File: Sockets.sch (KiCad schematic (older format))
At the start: 53 parts

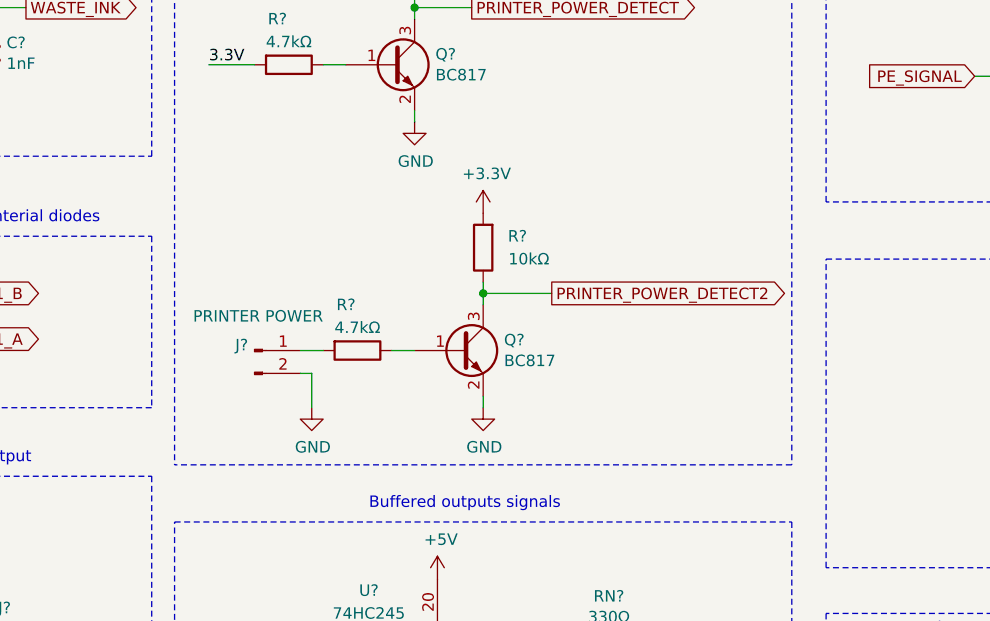
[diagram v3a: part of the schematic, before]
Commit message: Added USB B socket with ESD filter
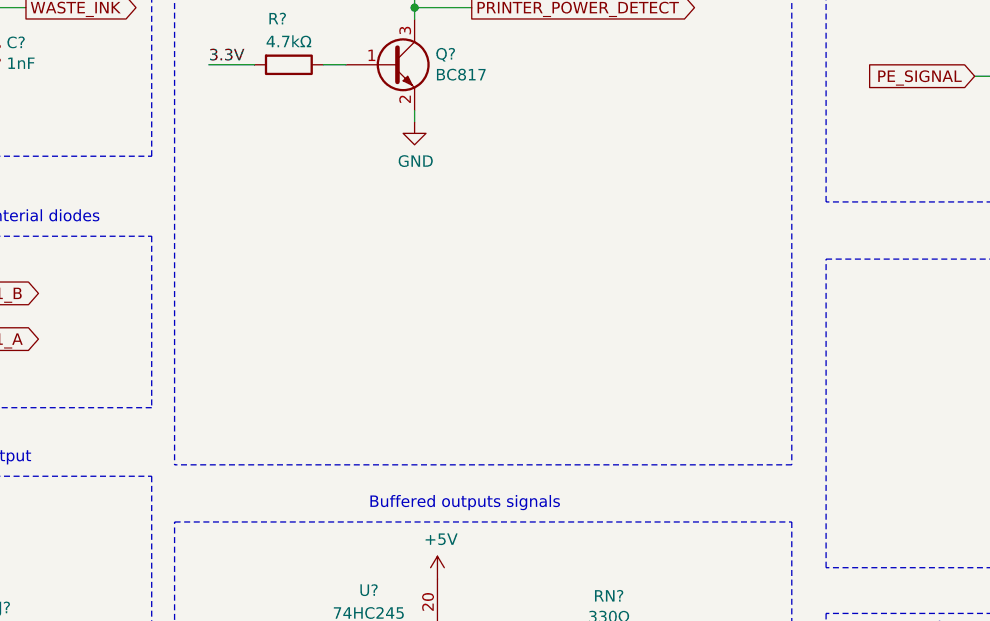
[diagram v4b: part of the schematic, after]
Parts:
- removed J?: PRINTER POWER, Connector_JST:JST_PH_B2B-PH-K_1x02_P2.00mm_Vertical, symbol Connector:Conn_01x02_Male
- removed Q?: BC817, Package_TO_SOT_SMD:SOT-23, symbol Transistor_BJT:BC817
- removed R?: 10kΩ, symbol Device:R
- removed R?: 4.7kΩ, symbol Device:R
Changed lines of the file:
@@
 	-1   0    0    -1
 $EndComp
-Text GLabel 2550 2650 2    50   Output ~ 0
-LIMIT_Y_FRONT
-Text GLabel 2500 3900 2    50   Output ~ 0
-LIMIT_Z_UP
-Text GLabel 2500 5150 2    50   Output ~ 0
-LIMIT_Z_DOWN
 Wire Wire Line
 	4500 3850 4550 3850
@@
 Text Label 2600 7000 0    50   ~ 0
 PE
-Wire Wire Line
-	6250 3000 6250 3150
-Wire Wire Line
-	6200 3000 6250 3000
-$Comp
-L power:GND #PWR?
-U 1 1 5E178011
-P 6250 3150
-AR Path="/5E07245F/5E178011" Ref="#PWR?"  Part="1"
-AR Path="/5E858220/5E178011" Ref="#PWR?"  Part="1"
-F 0 "#PWR?" H 6250 2900 50  0001 C CNN
-F 1 "GND" H 6255 2977 50  0000 C CNN
-F 2 "" H 6250 3150 50  0001 C CNN
-F 3 "" H 6250 3150 50  0001 C CNN
-	1    6250 3150
-	1    0    0    -1
-$EndComp
-Wire Wire Line
-	6200 2900 6300 2900
-Text GLabel 7300 2650 2    50   Output ~ 0
-PRINTER_POWER_DETECT2
-$Comp
-L power:+3.3V #PWR?
-U 1 1 5E168635
-P 7000 2300
-AR Path="/5E07245F/5E168635" Ref="#PWR?"  Part="1"
-AR Path="/5E858220/5E168635" Ref="#PWR?"  Part="1"
-F 0 "#PWR?" H 7000 2150 50  0001 C CNN
-F 1 "+3.3V" H 7015 2473 50  0000 C CNN
-F 2 "" H 7000 2300 50  0001 C CNN
-F 3 "" H 7000 2300 50  0001 C CNN
-	1    7000 2300
-	1    0    0    -1
-$EndComp
-$Comp
-L Device:R R?
-U 1 1 5E168627
-P 6450 2900
-AR Path="/5E07245F/5E168627" Ref="R?"  Part="1"
-AR Path="/5E858220/5E168627" Ref="R?"  Part="1"
-F 0 "R?" V 6250 2850 50  0000 C CNN
-F 1 "4.7kΩ" V 6350 2900 50  0000 C CNN
-F 2 "" V 6380 2900 50  0001 C CNN
-F 3 "~" H 6450 2900 50  0001 C CNN
-	1    6450 2900
-	0    1    1    0
-$EndComp
-Wire Wire Line
-	7000 2650 7000 2700
-Connection ~ 7000 2650
-Wire Wire Line
-	7000 2650 7300 2650
-$Comp
-L power:GND #PWR?
-U 1 1 5E16860A
-P 7000 3150
-AR Path="/5E07245F/5E16860A" Ref="#PWR?"  Part="1"
-AR Path="/5E858220/5E16860A" Ref="#PWR?"  Part="1"
-F 0 "#PWR?" H 7000 2900 50  0001 C CNN
-F 1 "GND" H 7005 2977 50  0000 C CNN
-F 2 "" H 7000 3150 50  0001 C CNN
-F 3 "" H 7000 3150 50  0001 C CNN
-	1    7000 3150
-	1    0    0    -1
-$EndComp
-Wire Wire Line
-	7000 2600 7000 2650
-$Comp
-L Device:R R?
-U 1 1 5E1685FF
-P 7000 2450
-AR Path="/5E07245F/5E1685FF" Ref="R?"  Part="1"
-AR Path="/5E858220/5E1685FF" Ref="R?"  Part="1"
-F 0 "R?" H 6850 2400 50  0000 C CNN
-F 1 "10kΩ" H 6800 2500 50  0000 C CNN
-F 2 "" V 6930 2450 50  0001 C CNN
-F 3 "~" H 7000 2450 50  0001 C CNN
-	1    7000 2450
-	-1   0    0    1
-$EndComp
-$Comp
-L Connector:Conn_01x02_Male J?
-U 1 1 5E10548D
-P 6000 2900
-AR Path="/5E07245F/5E10548D" Ref="J?"  Part="1"
-AR Path="/5E858220/5E10548D" Ref="J?"  Part="1"
-F 0 "J?" H 5972 2924 50  0000 R CNN
-F 1 "PRINTER POWER" H 6300 3050 50  0000 R CNN
-F 2 "Connector_JST:JST_PH_B2B-PH-K_1x02_P2.00mm_Vertical" H 6000 2900 50  0001 C CNN
-F 3 "~" H 6000 2900 50  0001 C CNN
-	1    6000 2900
-	1    0    0    -1
-$EndComp
-Text GLabel 6950 1400 2    50   Output ~ 0
-PRINTER_POWER_DETECT
 $Comp
 L power:+3.3V #PWR?
@@
 	1    0    0    -1
 $EndComp
-Text GLabel 2550 1400 2    50   Output ~ 0
-LIMIT_Y_BACK
 $Comp
 L Connector:Conn_01x02_Male J?
@@
 Wire Wire Line
 	9550 1700 9650 1700
-$Comp
-L Transistor_BJT:BC817 Q?
-U 1 1 5E1685F5
-P 6900 2900
-AR Path="/5E07245F/5E1685F5" Ref="Q?"  Part="1"
-AR Path="/5E858220/5E1685F5" Ref="Q?"  Part="1"
-F 0 "Q?" H 7091 2946 50  0000 L CNN
-F 1 "BC817" H 7091 2855 50  0000 L CNN
-F 2 "Package_TO_SOT_SMD:SOT-23" H 7100 2825 50  0001 L CIN
-F 3 "http://www.fairchildsemi.com/ds/BC/BC817.pdf" H 6900 2900 50  0001 L CNN
-	1    6900 2900
-	1    0    0    -1
-$EndComp
-Wire Wire Line
-	6600 2900 6700 2900
-Wire Wire Line
-	7000 3100 7000 3150
 Wire Wire Line
 	6300 1650 6400 1650
@@
 	0    -1   -1   0
 $EndComp
+Text GLabel 2550 1400 2    50   Output ~ 0
+LIMIT_Y_BACK
+Text GLabel 2500 5150 2    50   Output ~ 0
+LIMIT_Z_DOWN
+Text GLabel 2500 3900 2    50   Output ~ 0
+LIMIT_Z_UP
+Text GLabel 2550 2650 2    50   Output ~ 0
+LIMIT_Y_FRONT
+Text GLabel 6950 1400 2    50   Output ~ 0
+PRINTER_POWER_DETECT
 $EndSCHEMATC

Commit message: Improve schematics add new elements
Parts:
- removed D?: BZT52C3V3-7-F, Diode_SMD:D_SOD-123, symbol Device:D_Zener_ALT
- removed F?: SN010-60, Fuse:Fuse_1206_3216Metric, symbol Device:Polyfuse
- removed J?: PHOTO SENSOR EMITER, Connector_JST:JST_PH_B2B-PH-K_1x02_P2.00mm_Vertical, symbol Connector:Conn_01x02_Male
- removed J?: PHOTO SENSOR RECEIVER, Connector_JST:JST_PH_B2B-PH-K_1x03_P2.00mm_Vertical, symbol Connector:Conn_01x03_Male
- removed R?: NI, Resistor_SMD:R_0603_1608Metric, symbol Device:R
- removed R? (x2): 10kΩ, Resistor_SMD:R_0603_1608Metric, symbol Device:R
- added C?: 0.1uF, Capacitor_SMD:C_0603_1608Metric, symbol Device:C
- added D?: 1N4448WS-7-F, Diode_SMD:D_SOD-323, symbol Device:D_ALT
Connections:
- net +5V: now also C?.1
- net GND: now also C?.2, D?.2 (A)
- net at Q?.1 (B), R?.1: now also D?.1 (K)
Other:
- note removed: "Limit out. voltage to 3.3V"
- note removed: "Mount just one 10k resistor for corect sensor type"
- note removed: "NPN Type"
- note removed: "Ovecurrent protection for LED and Sensors?"
- note removed: "PNP Type"
- note removed: "Photobarier sensor Input"
- moved on the sheet: Q?, R?

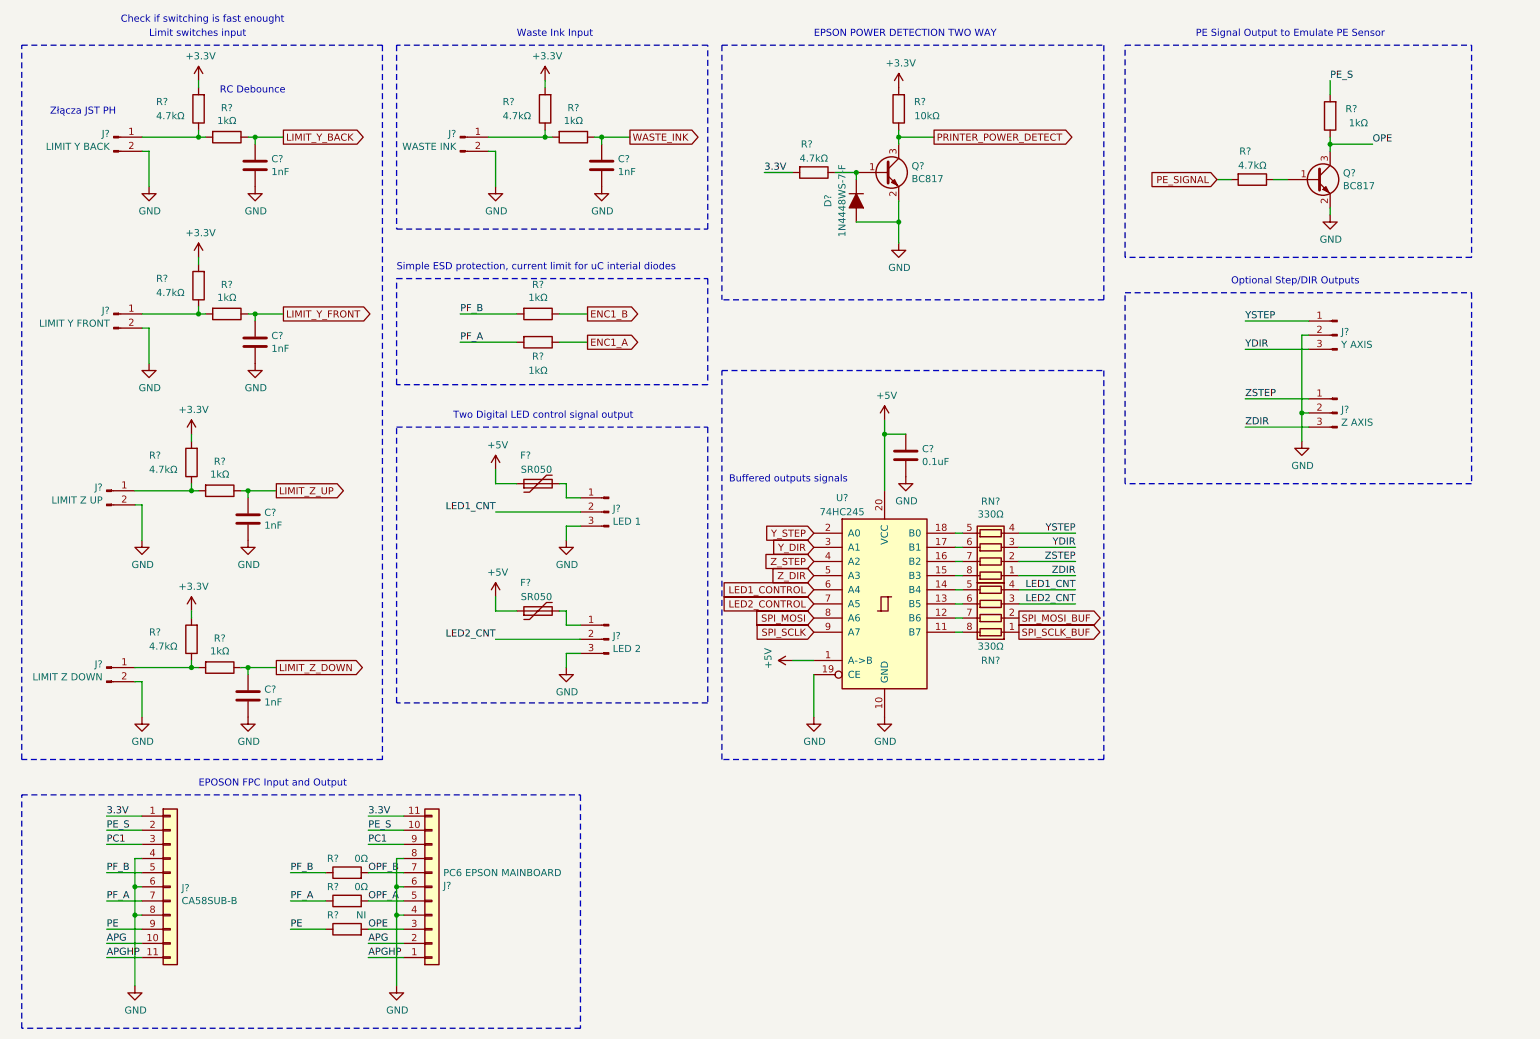
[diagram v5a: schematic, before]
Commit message: Numbering and finishing the schematic
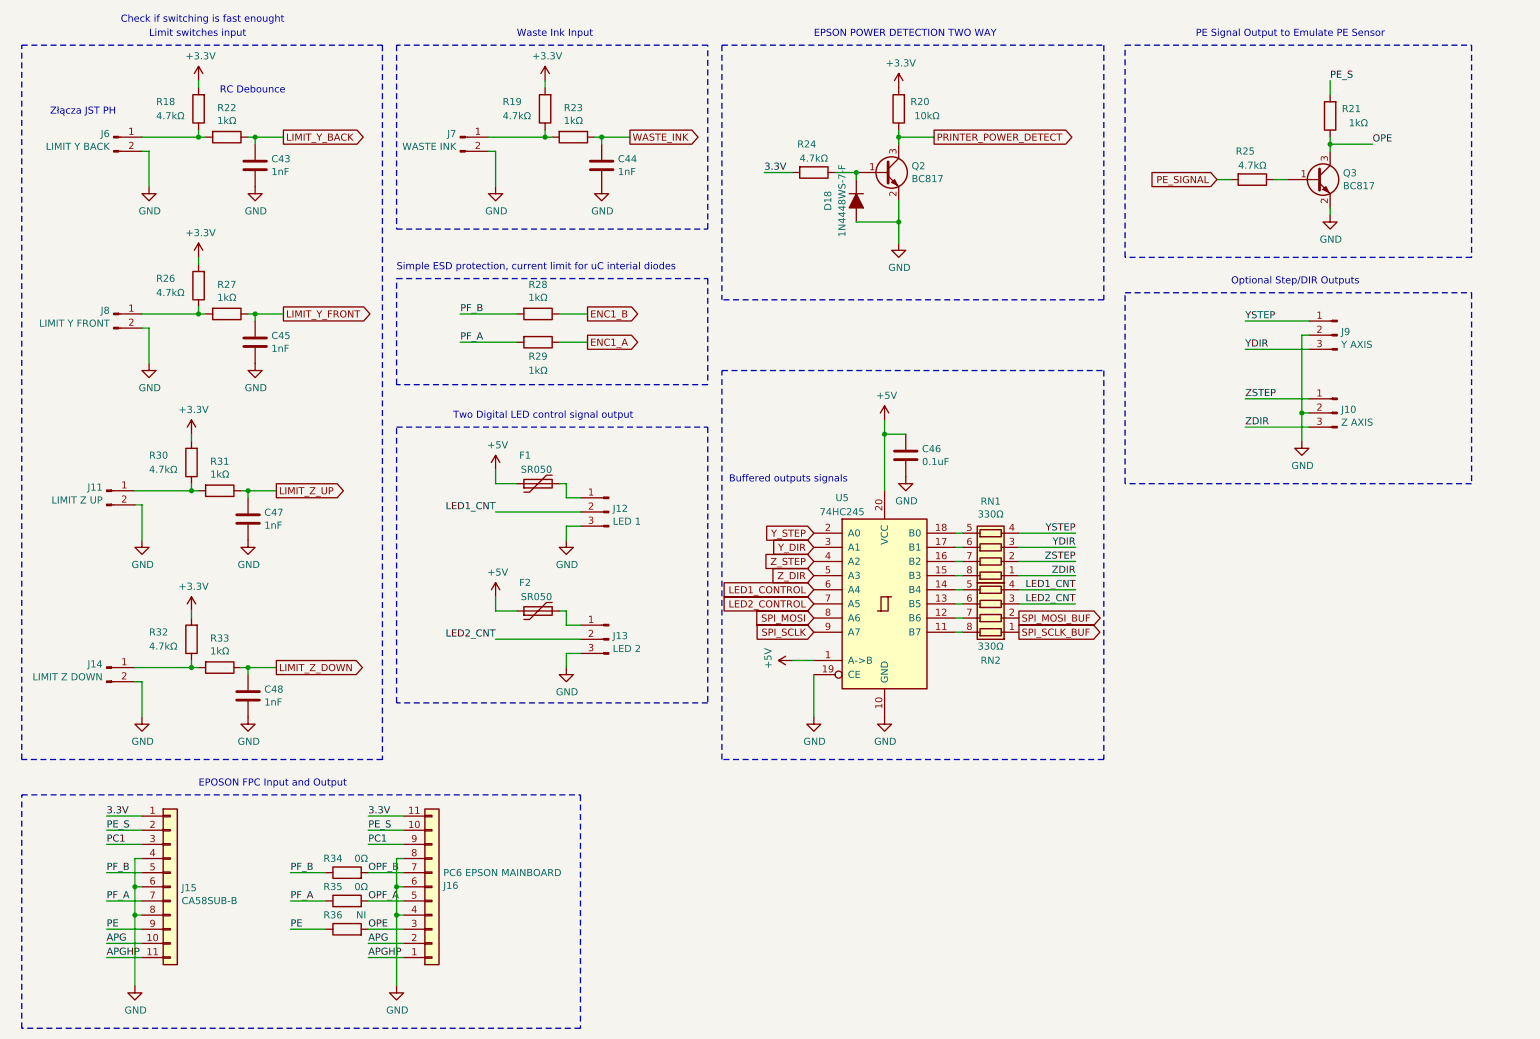
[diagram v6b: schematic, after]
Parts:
- gave numbers to parts that had none: 44

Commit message: Shematic almost finished, BOM in KiCad 3/4 finished
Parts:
- C48: renamed from C46; Cena (none) -> 0.05982; Dielektryk (none) -> X7R; Model (none) -> CL10B104KB8NNNC; Napięcie (none) -> 50V; Producent (none) -> SAMSUNG; Tolerancja (none) -> 10%; Typ (none) -> SMD
- D18: Cena (none) -> 0.14905; Link (none) -> https://www.tme.eu/pl/details/1n4448ws-7-f/diody-uniwersaln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; Model (none) -> 1N4448WS-7-F; Opis (none) -> Dioda: prostownicza; SMD; 75V; 0,25A; 4ns;; Producent (none) -> DIODES INCORPORATED; Typ (none) -> SMD
- F1, F2: Cena (none) -> 0.9060; Link (none) -> https://www.tme.eu/pl/details/sr050-06/bezpieczniki-polimer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; Model (none) -> SR050-06; Opis (none) -> Bezpiecznik: polimerowy PTC; 500mA; Obud: 0805; Producent (none) -> ECE; Typ (none) -> SMD
- J12: renamed from J7; Cena (none) -> 0.47429; Link (none) -> https://www.tme.eu/pl/details/b2b-ph-k-s/zlacza-sygnalowe-r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; Model (none) -> B2B-PH-K-S; Opis (none) -> Gniazdo; przewód-płytka; męskie; PH; 2mm; PIN: 2; THT; 100V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; Producent (none) -> JST; Typ (none) -> THT
- J13: renamed from J12; footprint Connector_JST:JST_PH_B2B-PH-K_1x03_P2.00mm_Vertical -> Connector_JST:JST_PH_B3B-PH-K_1x03_P2.00mm_Vertical; Cena (none) -> 0.59599; Link (none) -> https://www.tme.eu/pl/details/b3b-ph-k-s/zlacza-sygnalowe-r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; Model (none) -> B3B-PH-K-S; Opis (none) -> Gniazdo; przewód-płytka; męskie; PH; 2mm; PIN: 3; THT; 100V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; Producent (none) -> JST; Typ (none) -> THT
- J14: renamed from J13; footprint Connector_JST:JST_PH_B2B-PH-K_1x03_P2.00mm_Vertical -> Connector_JST:JST_PH_B3B-PH-K_1x03_P2.00mm_Vertical; Cena (none) -> 0.59599; Link (none) -> https://www.tme.eu/pl/details/b3b-ph-k-s/zlacza-sygnalowe-r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; Model (none) -> B3B-PH-K-S; Opis (none) -> Gniazdo; przewód-płytka; męskie; PH; 2mm; PIN: 3; THT; 100V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; Producent (none) -> JST; Typ (none) -> THT
- J15: renamed from J9; footprint Connector_JST:JST_PH_B2B-PH-K_1x03_P2.00mm_Vertical -> Connector_JST:JST_PH_B3B-PH-K_1x03_P2.00mm_Vertical; Cena (none) -> 0.59599; Link (none) -> https://www.tme.eu/pl/details/b3b-ph-k-s/zlacza-sygnalowe-r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; Model (none) -> B3B-PH-K-S; Opis (none) -> Gniazdo; przewód-płytka; męskie; PH; 2mm; PIN: 3; THT; 100V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; Producent (none) -> JST; Typ (none) -> THT
- J16: renamed from J10; footprint Connector_JST:JST_PH_B2B-PH-K_1x03_P2.00mm_Vertical -> Connector_JST:JST_PH_B3B-PH-K_1x03_P2.00mm_Vertical; Cena (none) -> 0.59599; Link (none) -> https://www.tme.eu/pl/details/b3b-ph-k-s/zlacza-sygnalowe-r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; Model (none) -> B3B-PH-K-S; Opis (none) -> Gniazdo; przewód-płytka; męskie; PH; 2mm; PIN: 3; THT; 100V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; Producent (none) -> JST; Typ (none) -> THT
- J6: renamed from J11; Cena (none) -> 0.47429; Link (none) -> https://www.tme.eu/pl/details/b2b-ph-k-s/zlacza-sygnalowe-r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; Model (none) -> B2B-PH-K-S; Opis (none) -> Gniazdo; przewód-płytka; męskie; PH; 2mm; PIN: 2; THT; 100V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; Producent (none) -> JST; Typ (none) -> THT
- J7: renamed from J14; Cena (none) -> 0.47429; Link (none) -> https://www.tme.eu/pl/details/b2b-ph-k-s/zlacza-sygnalowe-r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; Model (none) -> B2B-PH-K-S; Opis (none) -> Gniazdo; przewód-płytka; męskie; PH; 2mm; PIN: 2; THT; 100V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; Producent (none) -> JST; Typ (none) -> THT
- J8: renamed from J6; Cena (none) -> 0.47429; Link (none) -> https://www.tme.eu/pl/details/b2b-ph-k-s/zlacza-sygnalowe-r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; Model (none) -> B2B-PH-K-S; Opis (none) -> Gniazdo; przewód-płytka; męskie; PH; 2mm; PIN: 2; THT; 100V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; Producent (none) -> JST; Typ (none) -> THT
- J9: renamed from J8; Cena (none) -> 0.47429; Link (none) -> https://www.tme.eu/pl/details/b2b-ph-k-s/zlacza-sygnalowe-r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; Model (none) -> B2B-PH-K-S; Opis (none) -> Gniazdo; przewód-płytka; męskie; PH; 2mm; PIN: 2; THT; 100V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; Producent (none) -> JST; Typ (none) -> THT
- R26: renamed from R34; footprint (none) -> Resistor_SMD:R_0603_1608Metric
- R27: renamed from R35; footprint (none) -> Resistor_SMD:R_0603_1608Metric
- R28: renamed from R36; footprint (none) -> Resistor_SMD:R_0603_1608Metric
- R33: renamed from R24; footprint (none) -> Resistor_SMD:R_0603_1608Metric
- R34: renamed from R20; footprint (none) -> Resistor_SMD:R_0603_1608Metric
- R35: renamed from R25; footprint (none) -> Resistor_SMD:R_0603_1608Metric
- R36: renamed from R21; footprint (none) -> Resistor_SMD:R_0603_1608Metric
- RN1, RN2: footprint (none) -> Resistor_SMD:R_Array_Convex_4x0603; Cena (none) -> 0.04823; Link (none) -> https://www.tme.eu/pl/details/dr1206-330r-4_8/drabinki-rezy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; Model (none) -> 4D03WGJ0331T; Opis (none) -> Drabinka rezystorowa: Y; 330Ω; SMD; 1206; Il.rezystorów: 4;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; Producent (none) -> ROYAL OHM; Typ (none) -> SMD
- U5: footprint (none) -> Package_SO:TSSOP-20_4.4x6.5mm_P0.65mm; Cena (none) -> 0.9740; Link (none) -> https://www.tme.eu/pl/details/74hc245pw.112/bufory-nadajnik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; Model (none) -> 74HC245PW.112; Opis (none) -> IC: cyfrowy; bus transceiver; Kanały: 8; SMD; TSSOP20; Seri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; Producent (none) -> NEXPERIA; Typ (none) -> SMD
- renumbered C47 to C43, C48 to C44, C43 to C45, C45 to C46, C44 to C47, J15 to J10, J16 to J11, R30 to R18, R32 to R19, R18 to R20, R26 to R21, R31 to R22, R33 to R23, R22 to R24, R27 to R25, R28 to R29, R29 to R30, R19 to R31, R23 to R32

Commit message: BOM in KiCad almost finished, genereated NETLIST, create PCB
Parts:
- C43, C44, C45, C46, C47: Cena (none) -> 0.05563; Link (none) -> https://www.tme.eu/pl/details/cl10b102kb8nnnc/kondensatory-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; Model (none) -> CL10B102KB8NNNC; Opis (none) -> Kondensator: ceramiczny; MLCC; 1nF; 50V; X7R; ±10%; SMD; 06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; Producent (none) -> SAMSUNG; Typ (none) -> SMD
- Q2, Q3: Cena (none) -> 0.1189; Link (none) -> https://www.tme.eu/pl/details/bc817.215/tranzystory-npn-smd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; Model (none) -> BC817.215; Opis (none) -> Tranzystor: NPN; bipolarny; 45V; 0,5A; 250mW; SOT23; Producent (none) -> NEXPERIA; Typ (none) -> SMD
- R18, R19, R20, R21, R31, R33, R35: Cena (none) -> 0.04651; Link (none) -> https://www.tme.eu/pl/details/smd0603-4k7-1%25/rezystory-sm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; Model (none) -> SMD0603-4K7-1%; Opis (none) -> Rezystor: thick film; SMD; 0603; 4,7kΩ; 0,1W; ±1%; -55÷155°C; Producent (none) -> ROYAL OHM; Typ (none) -> SMD
- R22, R23, R24, R25, R29, R30, R32, R36: Cena (none) -> 0.04651; Link (none) -> https://www.tme.eu/pl/details/smd0603-1k-1%25/rezystory-smd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; Model (none) -> 0603SAF1001T5E; Opis (none) -> Rezystor: thick film; SMD; 0603; 1kΩ; 0,1W; ±1%; -55÷155°C; Producent (none) -> ROYAL OHM; Typ (none) -> SMD
- R26, R27, R28: Cena (none) -> 0.04651; Typ (none) -> SMD
- R34: Cena (none) -> 0.03622; Link (none) -> https://www.tme.eu/pl/details/smd0603-10k-1%25/rezystory-sm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; Model (none) -> 0603SAF1002T5E; Opis (none) -> Rezystor: thick film; SMD; 0603; 10kΩ; 0,1W; ±1%; -55÷155°C; Producent (none) -> ROYAL OHM; Typ (none) -> SMD
